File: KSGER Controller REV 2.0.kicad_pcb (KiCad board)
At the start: 2 copper layers, 114.3 x 40.6 mm, 51 parts, among them J1 24 VDC, J2 IRON_IN, J4 BATT, Q1 IRF7416, Q2 S8050, SW1 ENCODER, U1 STM32F103C8Tx, U2 AMS1117-3.3, U3 SGM8551, U4 24LC08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

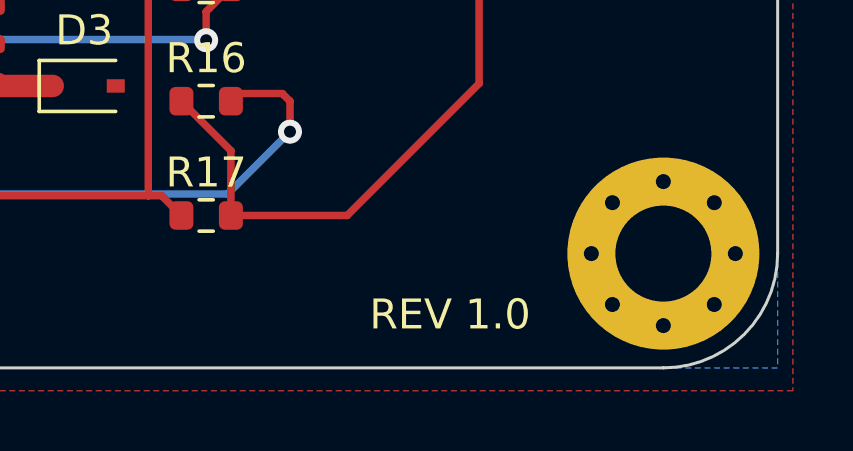
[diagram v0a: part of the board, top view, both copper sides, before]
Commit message: Created rev 2.0 to redo the board layout based on feedback on the EEVBlog forums
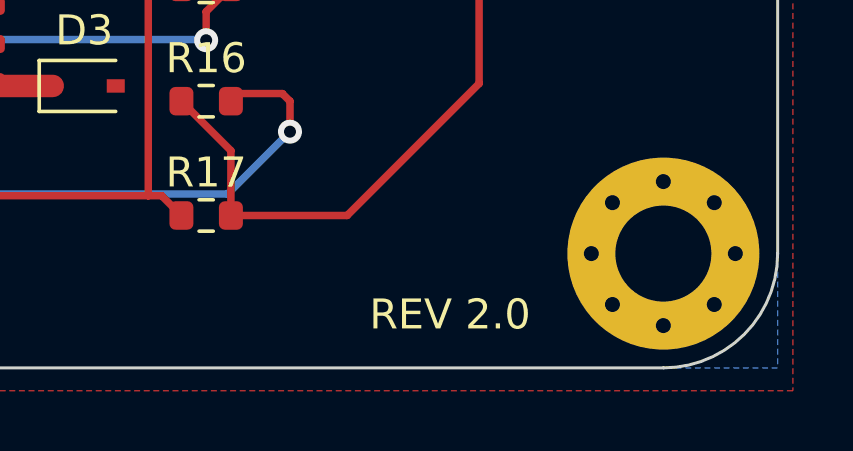
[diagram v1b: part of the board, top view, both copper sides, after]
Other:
- board text added: "REV 2.0"
- board text removed: "REV 1.0"
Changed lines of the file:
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@@
     (effects (font (size 1 1) (thickness 0.15)))
   )
-  (gr_text "REV 1.0" (at 192.278 116.332) (layer "F.SilkS")
+  (gr_text "REV 2.0" (at 192.278 116.332) (layer "F.SilkS")
     (effects (font (size 1 1) (thickness 0.12)))
   )

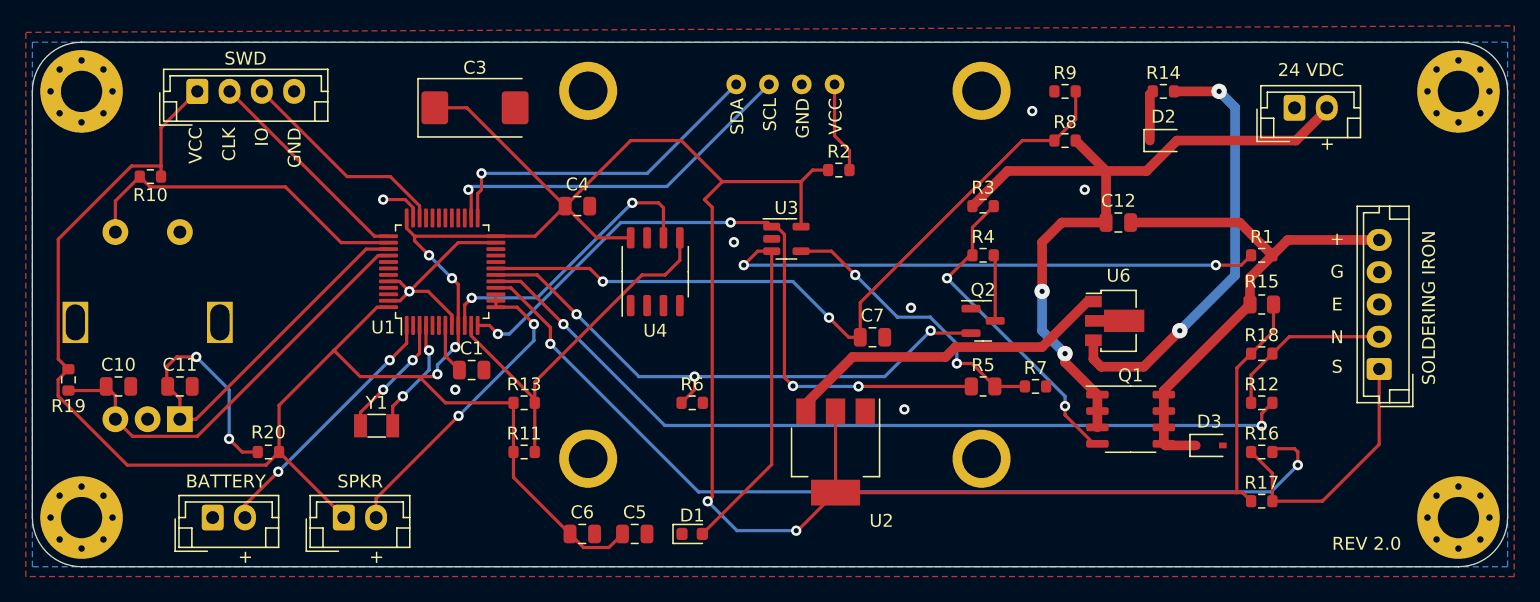
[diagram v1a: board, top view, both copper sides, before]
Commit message: Removed all traces to start from scratch!
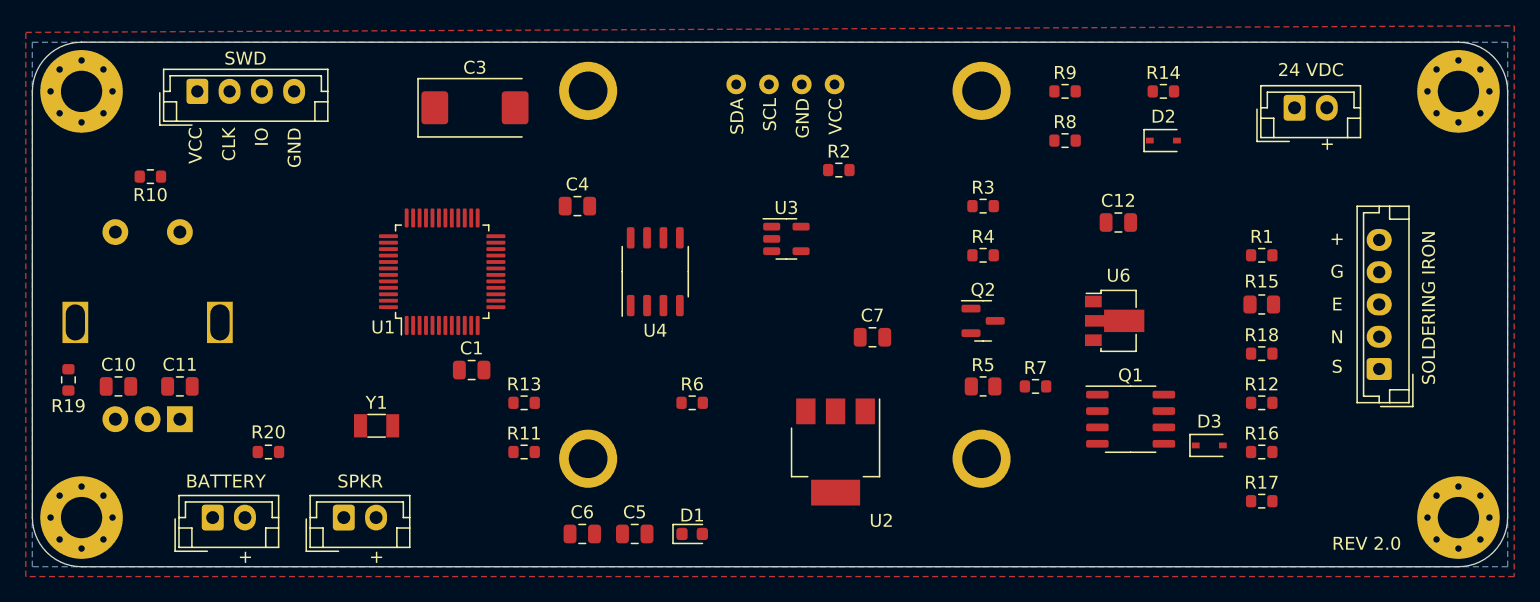
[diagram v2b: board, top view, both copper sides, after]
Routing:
- net +3V3: track 273.4 -> 0.00 mm, vias 6 -> 0
- net SHAKE: track 73.5 -> 0.00 mm, vias 2 -> 0
- net Net-(D1-Pad2): track 66.4 -> 0.00 mm, vias 2 -> 0
- net NTC: track 66.1 -> 0.00 mm, vias 2 -> 0
- net +24V: track 59.7 -> 0.00 mm, vias 2 -> 0
- net VIN_MON: track 57.9 -> 0.00 mm, vias 2 -> 0
- net TIP_TEMP: track 53.9 -> 0.00 mm, vias 4 -> 0
- net HEATER_ON: track 44.1 -> 0.00 mm, vias 3 -> 0
- net Net-(C12-Pad2): track 41.4 -> 0.00 mm
- net ENCODER_A: track 38.7 -> 0.00 mm, vias 2 -> 0
- net Net-(R14-Pad2): track 33.9 -> 0.00 mm, vias 2 -> 0
- net ENCODER_B: track 33.4 -> 0.00 mm
- net EE_SDA: track 30.1 -> 0.00 mm
- net OLED_SCL: track 28.9 -> 0.00 mm, vias 1 -> 0
- net ENCODER_SW: track 26.5 -> 0.00 mm
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
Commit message: Working on trace redesign for v2
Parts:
- added C2: 0.1, Capacitor_SMD:C_0201_0603Metric, F.Cu at (117.9, 89.2)
- added C8: 0.1, Capacitor_SMD:C_0201_0603Metric, F.Cu at (114.6, 98.0)
- added C9: 0.1, Capacitor_SMD:C_0201_0603Metric, F.Cu at (121.9, 101.3)
- C6: footprint Capacitor_SMD:C_0805_2012Metric -> Capacitor_SMD:C_0201_0603Metric
- moved C7 29.5 mm to (181.7, 90.4), turned to 180 degrees
- moved U2 27.6 mm to (173.3, 92.7), turned to 180 degrees
- moved C6 23.6 mm to (126.7, 92.5)
- moved C12 17.3 mm to (156.7, 85.9)
- moved R8 16.4 mm to (185.0, 88.4)
- moved R9 14.8 mm to (181.9, 88.4)
- moved U6 14.5 mm to (175.3, 84.8), turned to 180 degrees
- moved R18 12.0 mm to (188.0, 113.0)
- moved R1 12.0 mm to (188.0, 105.4)
- moved R15 12.0 mm to (188.0, 109.2)
- moved C1 7.64 mm to (130.4, 101.1)
- moved D2 6.49 mm to (182.9, 84.1), turned to 90 degrees
- moved J2 4.89 mm to (197.6, 105.1)
- moved J1 3.96 mm to (189.2, 85.6), turned to 90 degrees
- moved R14 3.65 mm to (178.9, 84.1), turned to 90 degrees
- renumbered JE to J5
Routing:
- net +24V: track 0.00 -> 14.4 mm
- net +3V3: track 0.00 -> 6.43 mm
- net Net-(U2-Pad3): track 0.00 -> 4.29 mm
- net Net-(D2-Pad1): track 0.00 -> 4.16 mm
- net VIN_MON: track 0.00 -> 3.49 mm
- net Net-(R14-Pad2): track 0.00 -> 1.94 mm
